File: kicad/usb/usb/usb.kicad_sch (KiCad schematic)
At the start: 19 parts, among them J1 USB_C_Receptacle_USB2.0_14P, J2 PH1.25mm 2P, J3 Conn_01x07_Pin, Q1 BSS84, SW1 PWR, U1 S-T111B33MC-OGSTFU, U2 MCP73831-2-OT

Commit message: Various kicad edits
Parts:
- J2: value PH1.25mm 2P -> PH2.0mm 2P; footprint Connector_JST:JST_GH_SM02B-GHS-TB_1x02-1MP_P1.25mm_Horizontal -> Connector_JST:JST_PH_S2B-PH-K_1x02_P2.00mm_Horizontal
- SW1: footprint Button_Switch_SMD:SW_SPDT_Shouhan_MSK12C02 -> Button_Switch_THT:SW_Slide_SPDT_Angled_CK_OS102011MA1Q
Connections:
- net VBAT: now also SW1.3 (C); no longer SW1.2 (B)
- net VSENSE: now also SW1.2 (B); no longer SW1.1 (A)
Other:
- moved on the sheet: C1, C2, C3, C4, C5, J1, J2, J3, Q1, R1, R2, R3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

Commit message: Adjusted parts & traces on usb kicad
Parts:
- C5: footprint Capacitor_SMD:C_0805_2012Metric -> Capacitor_SMD:C_0603_1608Metric_Pad1.08x0.95mm_HandSolder
- R1: footprint Resistor_SMD:R_0402_1005Metric_Pad0.72x0.64mm_HandSolder -> Resistor_SMD:R_0603_1608Metric_Pad0.98x0.95mm_HandSolder
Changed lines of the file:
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@@
 			)
 		)
-		(property "Footprint" "Capacitor_SMD:C_0805_2012Metric"
+		(property "Footprint" "Capacitor_SMD:C_0603_1608Metric_Pad1.08x0.95mm_HandSolder"
 			(at 29.21 74.6252 0)
 			(effects
@@
 			)
 		)
-		(property "Footprint" "Resistor_SMD:R_0402_1005Metric_Pad0.72x0.64mm_HandSolder"
+		(property "Footprint" "Resistor_SMD:R_0603_1608Metric_Pad0.98x0.95mm_HandSolder"
 			(at 33.02 71.628 90)
 			(effects

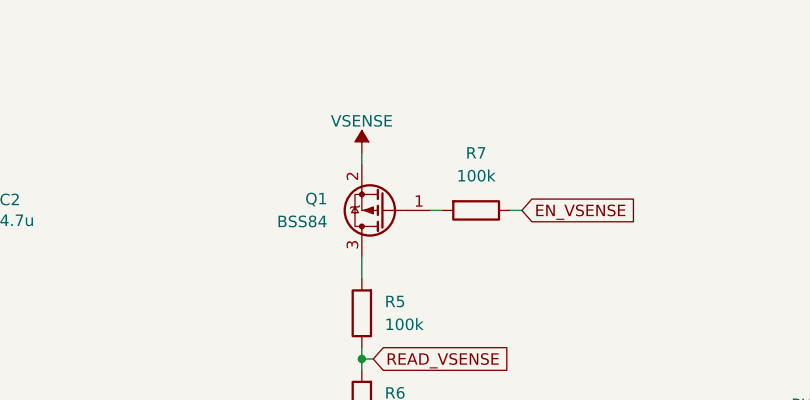
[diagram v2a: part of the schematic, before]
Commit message: Added pulldown resistor, made vsense enable always on
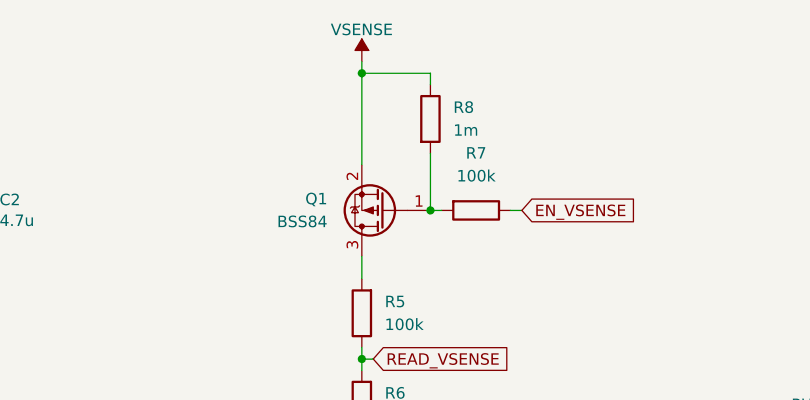
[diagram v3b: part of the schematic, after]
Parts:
- added R8: 1m, Resistor_SMD:R_0402_1005Metric_Pad0.72x0.64mm_HandSolder, symbol Device:R
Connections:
- net VSENSE: now also R8.1
- net at Q1.1 (G), R7.2: now also R8.2
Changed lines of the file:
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@@
 	(paper "A4")
 	(junction
+		(at 167.64 39.37)
+		(diameter 0)
+		(color 0 0 0 0)
+	)
+	(junction
 		(at 36.83 68.58)
 		(diameter 0)
@@
 	)
 	(junction
+		(at 160.02 24.13)
+		(diameter 0)
+		(color 0 0 0 0)
+	)
+	(junction
 		(at 184.15 118.11)
 		(diameter 0)
@@
 	(wire
 		(pts
-			(xy 160.02 33.02) (xy 160.02 34.29)
+			(xy 160.02 24.13) (xy 160.02 34.29)
+		)
+		(stroke
+			(width 0)
+			(type default)
+		)
+	)
+	(wire
+		(pts
+			(xy 167.64 24.13) (xy 167.64 25.4)
 		)
 		(stroke
@@
 	(wire
 		(pts
+			(xy 160.02 24.13) (xy 167.64 24.13)
+		)
+		(stroke
+			(width 0)
+			(type default)
+		)
+	)
+	(wire
+		(pts
 			(xy 160.02 55.88) (xy 160.02 57.15)
 		)
@@
 	(wire
 		(pts
+			(xy 167.64 33.02) (xy 167.64 39.37)
+		)
+		(stroke
+			(width 0)
+			(type default)
+		)
+	)
+	(wire
+		(pts
 			(xy 82.55 49.53) (xy 82.55 52.07)
 		)
@@
 	(wire
 		(pts
+			(xy 160.02 22.86) (xy 160.02 24.13)
+		)
+		(stroke
+			(width 0)
+			(type default)
+		)
+	)
+	(wire
+		(pts
 			(xy 69.85 34.29) (xy 69.85 36.83)
 		)
@@
 	(symbol
 		(lib_id "power:VCOM")
-		(at 160.02 33.02 0)
+		(at 160.02 22.86 0)
 		(unit 1)
 		(exclude_from_sim no)
@@
 		(dnp no)
 		(property "Reference" "#PWR04"
-			(at 160.02 36.83 0)
+			(at 160.02 26.67 0)
 			(effects
 				(font
@@
 		)
 		(property "Value" "VSENSE"
-			(at 160.02 29.464 0)
+			(at 160.02 19.304 0)
 			(effects
 				(font
@@
 		)
 		(property "Footprint" ""
-			(at 160.02 33.02 0)
+			(at 160.02 22.86 0)
 			(effects
 				(font
@@
 		)
 		(property "Datasheet" ""
-			(at 160.02 33.02 0)
+			(at 160.02 22.86 0)
 			(effects
 				(font
@@
 		)
 		(property "Description" "Power symbol creates a global label with name \"VCOM\""
-			(at 160.02 33.02 0)
+			(at 160.02 22.86 0)
 			(effects
 				(font
@@
 					(unit 1)
 				)
+			)
+		)
+	)
+	(symbol
+		(lib_id "Device:R")
+		(at 167.64 29.21 0)
+		(unit 1)
+		(exclude_from_sim no)
+		(in_bom yes)
+		(on_board yes)
+		(dnp no)
+		(fields_autoplaced yes)
+		(property "Reference" "R8"
+			(at 170.18 27.9399 0)
+			(effects
+				(font
+					(size 1.27 1.27)
+				)
+				(justify left)
+			)
+		)
+		(property "Value" "1m"
+			(at 170.18 30.4799 0)
+			(effects
+				(font
+					(size 1.27 1.27)
+				)
+				(justify left)
+			)
+		)
+		(property "Footprint" "Resistor_SMD:R_0402_1005Metric_Pad0.72x0.64mm_HandSolder"
+			(at 165.862 29.21 90)
+			(effects
+				(font
+					(size 1.27 1.27)
+				)
+				(hide yes)
+			)
+		)
+		(property "Datasheet" "~"
+			(at 167.64 29.21 0)
+			(effects
+				(font
+					(size 1.27 1.27)
+				)
+				(hide yes)
+			)
+		)
+		(property "Description" "Resistor"
+			(at 167.64 29.21 0)
+			(effects
+				(font
+					(size 1.27 1.27)
+				)
+				(hide yes)
+			)
+		)
+		(pin "1"
+		)
+		(pin "2"
+		)
+		(instances
+			(project "usb"
+				(path "/04b8416f-1444-47df-9f1d-0c05dd751dad"
+					(reference "R8")
+					(unit 1)
+				)

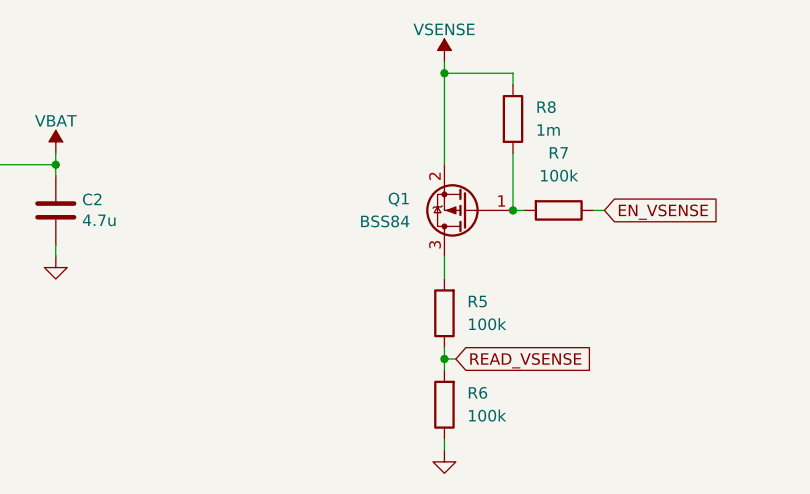
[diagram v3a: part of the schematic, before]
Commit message: Swapped the p-channel mosfet for a pnp transistor
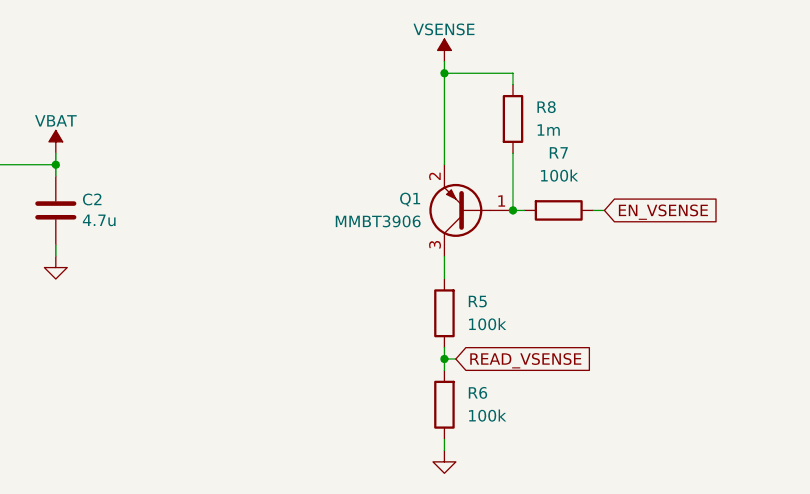
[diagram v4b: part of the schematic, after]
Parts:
- removed Q1: BSS84, Package_TO_SOT_SMD:SOT-23, symbol Transistor_FET:BSS84
- added Q1: MMBT3906, Package_TO_SOT_SMD:SOT-23, symbol Transistor_BJT:MMBT3906
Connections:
- net VSENSE: now also Q1.2 (E)
- net at R5.2: now also Q1.3 (C)
- net at R7.2, R8.2: now also Q1.1 (B)
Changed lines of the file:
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@@
 	(paper "A4")
 	(junction
-		(at 167.64 39.37)
-		(diameter 0)
-		(color 0 0 0 0)
-	)
-	(junction
 		(at 36.83 68.58)
 		(diameter 0)
@@
 	)
 	(junction
+		(at 167.64 39.37)
+		(diameter 0)
+		(color 0 0 0 0)
+	)
+	(junction
 		(at 29.21 69.85)
 		(diameter 0)
@@
 	)
 	(symbol
+		(lib_id "Transistor_BJT:MMBT3906")
+		(at 162.56 39.37 180)
+		(unit 1)
+		(exclude_from_sim no)
+		(in_bom yes)
+		(on_board yes)
+		(dnp no)
+		(fields_autoplaced yes)
+		(property "Reference" "Q1"
+			(at 157.48 38.0999 0)
+			(effects
+				(font
+					(size 1.27 1.27)
+				)
+				(justify left)
+			)
+		)
+		(property "Value" "MMBT3906"
+			(at 157.48 40.6399 0)
+			(effects
+				(font
+					(size 1.27 1.27)
+				)
+				(justify left)
+			)
+		)
+		(property "Footprint" "Package_TO_SOT_SMD:SOT-23"
+			(at 157.48 37.465 0)
+			(effects
+				(font
+					(size 1.27 1.27)
+					(italic yes)
+				)
+				(justify left)
+				(hide yes)
+			)
+		)
+		(property "Datasheet" "https://www.onsemi.com/pdf/datasheet/pzt3906-d.pdf"
+			(at 162.56 39.37 0)
+			(effects
+				(font
+					(size 1.27 1.27)
+				)
+				(justify left)
+				(hide yes)
+			)
+		)
+		(property "Description" "-0.2A Ic, -40V Vce, Small Signal PNP Transistor, SOT-23"
+			(at 162.56 39.37 0)
+			(effects
+				(font
+					(size 1.27 1.27)
+				)
+				(hide yes)
+			)
+		)
+		(pin "1"
+		)
+		(pin "2"
+		)
+		(pin "3"
+		)
+		(instances
+			(project ""
+				(path "/04b8416f-1444-47df-9f1d-0c05dd751dad"
+					(reference "Q1")
+					(unit 1)
+				)
+			)
+		)
+	)
+	(symbol
 		(lib_id "power:VCOM")
 		(at 116.84 33.02 0)
@@
 					(unit 1)
 				)
-			)
-		)
-	)
-	(symbol
-		(lib_id "Transistor_FET:BSS84")
-		(at 162.56 39.37 180)
-		(unit 1)
-		(exclude_from_sim no)
-		(in_bom yes)
-		(on_board yes)
-		(dnp no)
-		(fields_autoplaced yes)
-		(property "Reference" "Q1"
-			(at 156.21 38.0999 0)
-			(effects
-				(font
-					(size 1.27 1.27)
-				)
-				(justify left)
-			)
-		)
-		(property "Value" "BSS84"
-			(at 156.21 40.6399 0)
-			(effects
-				(font
-					(size 1.27 1.27)
-				)
-				(justify left)
-			)
-		)
-		(property "Footprint" "Package_TO_SOT_SMD:SOT-23"
-			(at 157.48 37.465 0)
-			(effects
-				(font
-					(size 1.27 1.27)
-					(italic yes)
-				)
-				(justify left)
-				(hide yes)
-			)
-		)
-		(property "Datasheet" "http://assets.nexperia.com/documents/data-sheet/BSS84.pdf"
-			(at 157.48 35.56 0)
-			(effects
-				(font
-					(size 1.27 1.27)
-				)
-				(justify left)
-				(hide yes)
-			)
-		)
-		(property "Description" "-0.13A Id, -50V Vds, P-Channel MOSFET, SOT-23"
-			(at 162.56 39.37 0)
-			(effects
-				(font
-					(size 1.27 1.27)
-				)
-				(hide yes)
-			)
-		)
-		(pin "3"
-		)
-		(pin "2"
-		)
-		(pin "1"
-		)
-		(instances
-			(project ""
-				(path "/04b8416f-1444-47df-9f1d-0c05dd751dad"
-					(reference "Q1")
-					(unit 1)
-				)
